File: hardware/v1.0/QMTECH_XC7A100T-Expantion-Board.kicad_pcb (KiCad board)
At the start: 4 copper layers, 98.2 x 98.2 mm, 117 parts, among them J1 Conn_01x34, J2 Conn_01x03, J3 Conn_01x04, J4 Conn_01x03, J5 Conn_01x34, J6 Conn_01x34, J7 Conn_01x34, J9 Conn_01x06, U2 AMS1117-1.8, U3 ADV7180BCP32Z-RL, U4 TLV62585, U5 74LVC245A, U6 TLV62585, U7 74LVC245A, U8 74LVC245A, U9 74LVC245A, Y1 28.63636MHz

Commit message: backup
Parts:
- removed D4: GREEN, LED_SMD:LED_0402_1005Metric_Pad0.77x0.64mm_HandSolder
- removed J1: Conn_01x34, C279718:FPC-SMD_KH-FG0.5-H2.0-34PIN
- removed J3: Conn_01x04, Connector_PinHeader_2.54mm:PinHeader_1x04_P2.54mm_Vertical
- removed RN21, RN22, RN23, RN24, RN27, RN28, RN29, RN30, RN31, RN32, RN33, RN34: 270, Resistor_SMD:R_Array_Convex_4x0603
- removed RN25, RN26: 540, Resistor_SMD:R_Array_Convex_4x0603
- added C36: 22uf, Capacitor_SMD:C_0805_2012Metric, F.Cu at (165.3, 117.7)
- added C37: 22uf, Capacitor_SMD:C_0805_2012Metric, F.Cu at (165.3, 120.7)
- added C38: 10nf, Capacitor_SMD:C_0603_1608Metric, F.Cu at (158.0, 175.1)
- added C39: 22uf, Capacitor_SMD:C_0805_2012Metric, F.Cu at (165.3, 123.7)
- added J10: Conn_01x06, Connector_PinHeader_2.54mm:PinHeader_1x06_P2.54mm_Vertical, F.Cu at (78.7, 136.5)
- added J11: Conn_01x04, Connector_PinHeader_2.54mm:PinHeader_1x04_P2.54mm_Vertical, F.Cu at (129.5, 111.8)
- added J12: Conn_01x34, C279718:FPC-SMD_KH-FG0.5-H2.0-34PIN, F.Cu at (142.9, 113.6)
- added J13: Conn_02x10_Odd_Even, Connector_PinSocket_2.54mm:PinSocket_2x10_P2.54mm_Vertical, F.Cu at (154.8, 136.5)
- added J8: Conn_01x34, C279718:FPC-SMD_KH-FG0.5-H2.0-34PIN, F.Cu at (110.9, 113.7)
- added L3: 1uh, Inductor_SMD:L_0603_1608Metric, F.Cu at (169.5, 117.5)
- added R24: 270, Resistor_SMD:R_0603_1608Metric, F.Cu at (-18.8, 143.9)
- added R25: 270, Resistor_SMD:R_0603_1608Metric, F.Cu at (-22.6, 201.8)
- added R26: 270, Resistor_SMD:R_0603_1608Metric, F.Cu at (-22.6, 204.3)
- added R27: 270, Resistor_SMD:R_0603_1608Metric, F.Cu at (-21.0, 172.7)
- added R28: 4.7K, Resistor_SMD:R_0603_1608Metric, B.Cu at (132.5, 114.3)
- added R29: 4.7K, Resistor_SMD:R_0603_1608Metric, B.Cu at (132.5, 116.8)
- added R30: 270, Resistor_SMD:R_0603_1608Metric, F.Cu at (158.0, 182.7)
- added R31: 450K, Resistor_SMD:R_0402_1005Metric, F.Cu at (169.0, 119.7)
- added R32: 100K, Resistor_SMD:R_0402_1005Metric, F.Cu at (169.0, 121.7)
- added R33: 20, Resistor_SMD:R_0603_1608Metric, F.Cu at (170.6, 176.9)
- added U10: 74LVC245A, Package_SO:TSSOP-20_4.4x6.5mm_P0.65mm, F.Cu at (77.1, 123.2)
- added U11: TLV62585, Package_TO_SOT_SMD:SOT-563, F.Cu at (171.3, 124.8)
- C10, C17: value 10nf -> 22uf; footprint Capacitor_SMD:C_0603_1608Metric -> Capacitor_SMD:C_0805_2012Metric
- C11: value 82nf -> 0.1uf
- C13, C14: value 0.1uf -> 10nf
- C19: value 10nf -> 82nf
- C2, C3: value 0.1uf -> 47pf
- C21: value 22uf -> 0.1uf; footprint Capacitor_SMD:C_0805_2012Metric -> Capacitor_SMD:C_0603_1608Metric
- C22: value 22uf -> 10nf; footprint Capacitor_SMD:C_0805_2012Metric -> Capacitor_SMD:C_0603_1608Metric
- C25, C26, C27, C28, C29, L2: moved to B.Cu
- C5, C6: value 47pf -> 0.1uf; moved to B.Cu
- D2: value LED -> GREEN; footprint LED_SMD:LED_0805_2012Metric -> LED_SMD:LED_0402_1005Metric_Pad0.77x0.64mm_HandSolder
- D3: value GREEN -> LED; footprint LED_SMD:LED_0402_1005Metric_Pad0.77x0.64mm_HandSolder -> LED_SMD:LED_0805_2012Metric
- J2, J4: value Conn_01x03 -> Conn_01x34; footprint Connector_PinHeader_2.54mm:PinHeader_1x03_P2.54mm_Vertical -> C279718:FPC-SMD_KH-FG0.5-H2.0-34PIN
- J5, J6: value Conn_01x34 -> Conn_01x03; footprint C279718:FPC-SMD_KH-FG0.5-H2.0-34PIN -> Connector_PinHeader_2.54mm:PinHeader_1x03_P2.54mm_Vertical
- J7: value Conn_01x34 -> Conn_01x04; footprint C279718:FPC-SMD_KH-FG0.5-H2.0-34PIN -> Connector_PinHeader_2.54mm:PinHeader_1x04_P2.54mm_Vertical
- J9: value Conn_01x06 -> Conn_01x34; footprint Connector_PinHeader_2.54mm:PinHeader_1x06_P2.54mm_Vertical -> C279718:FPC-SMD_KH-FG0.5-H2.0-34PIN
- R1, R2: value 36 -> 4.7K; footprint Resistor_SMD:R_0603_1608Metric -> Resistor_SMD:R_0603_1608Metric_Pad0.98x0.95mm_HandSolder
- R10: value 450K -> 36; footprint Resistor_SMD:R_0402_1005Metric -> Resistor_SMD:R_0603_1608Metric; moved to B.Cu
- R11: value 100K -> 39; footprint Resistor_SMD:R_0402_1005Metric -> Resistor_SMD:R_0603_1608Metric; moved to B.Cu
- R12: value 100 -> 39; moved to B.Cu
- R13: value 100 -> 270
- R14: value 1K -> 1.69k
- R15: value 10K -> 450K; footprint Resistor_SMD:R_0603_1608Metric -> Resistor_SMD:R_0402_1005Metric
- R16: value 450K -> 100K
- R17: value 100K -> 100; footprint Resistor_SMD:R_0402_1005Metric -> Resistor_SMD:R_0603_1608Metric; moved to B.Cu
- R18: value 270 -> 100; moved to B.Cu
- R19: value 270 -> 1K
- R20: value 270 -> 450K; footprint Resistor_SMD:R_0603_1608Metric -> Resistor_SMD:R_0402_1005Metric; moved to B.Cu
- R21: value 270 -> 100K; footprint Resistor_SMD:R_0603_1608Metric -> Resistor_SMD:R_0402_1005Metric; moved to B.Cu
- R3, R4: value 39 -> 4.7K; footprint Resistor_SMD:R_0603_1608Metric -> Resistor_SMD:R_0603_1608Metric_Pad0.98x0.95mm_HandSolder
- R5: value 10K -> 4.7K; footprint Resistor_SMD:R_0603_1608Metric -> Resistor_SMD:R_0603_1608Metric_Pad0.98x0.95mm_HandSolder
- R6, R7: value 270 -> 4.7K; footprint Resistor_SMD:R_0603_1608Metric -> Resistor_SMD:R_0603_1608Metric_Pad0.98x0.95mm_HandSolder
- R8: value 270 -> 10K
- R9: value 1.69k -> 36; moved to B.Cu
- RN10, RN13, RN14, RN9: value 270 -> 540
- RN15, RN16: value 540 -> 270
- RN17, RN18, RN19, RN20: value 270 -> 0
- U2: value AMS1117-1.8 -> CP2102N-Axx-xQFN24; footprint Package_TO_SOT_SMD:SOT-223-3_TabPin2 -> Package_DFN_QFN:QFN-24-1EP_4x4mm_P0.5mm_EP2.6x2.6mm
- U3: value ADV7180BCP32Z-RL -> AMS1117-1.8; footprint Package_CSP:LFCSP-32-1EP_5x5mm_P0.5mm_EP3.6x3.6mm -> Package_TO_SOT_SMD:SOT-223-3_TabPin2
- U4: value TLV62585 -> ADV7180BCP32Z-RL; footprint Package_TO_SOT_SMD:SOT-563 -> Package_CSP:LFCSP-32-1EP_5x5mm_P0.5mm_EP3.6x3.6mm
- U5: value 74LVC245A -> TLV62585; footprint Package_SO:TSSOP-20_4.4x6.5mm_P0.65mm -> Package_TO_SOT_SMD:SOT-563
- U6: value TLV62585 -> 74LVC245A; footprint Package_TO_SOT_SMD:SOT-563 -> Package_SO:TSSOP-20_4.4x6.5mm_P0.65mm; moved to B.Cu
- U7: value 74LVC245A -> TLV62585; footprint Package_SO:TSSOP-20_4.4x6.5mm_P0.65mm -> Package_TO_SOT_SMD:SOT-563; moved to B.Cu
- moved C30 293.2 mm to (-18.8, 136.4)
- moved C31 293.2 mm to (-18.8, 138.9)
- moved D2 241.2 mm to (11.9, 197.9)
- moved C32 236.5 mm to (-22.6, 196.7)
- moved C33 236.5 mm to (-22.6, 199.2)
- moved R19 232.4 mm to (46.0, 179.7)
- moved C34 232.3 mm to (-21.0, 167.7)
- moved C35 232.3 mm to (-21.0, 170.2)
- moved RN8 223.3 mm to (64.0, 135.4), turned to 90 degrees
- moved R23 220.6 mm to (-18.8, 141.4)
- moved C23 219.5 mm to (46.8, 187.5)
- moved C24 219.5 mm to (46.8, 190.5)
- moved U7 216.8 mm to (64.3, 126.1), turned to 180 degrees
- moved RN14 216.6 mm to (74.4, 129.2), turned to 90 degrees
- moved RN7 215.2 mm to (68.0, 135.4), turned to 90 degrees
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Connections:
- C10 pad 1: +1V8 -> +5V
- C10 pad 2: Net-(U3-ELPF) -> GND
- C11 pad 1: +1V8 -> +3V3
- C11 pad 2: Net-(C11-Pad2) -> GND
- C12 pad 1: +3V3 -> +1V8
- C13 pad 1: +1V8 -> +3V3
- C16 pad 1: +3V3 -> +1V8
- C17 pad 1: +1V8 -> +3V3
- C18 pad 2: GND -> Net-(U4-ELPF)
- C19 pad 2: GND -> Net-(C19-Pad2)
- C2 pad 1: +3V3 -> Net-(U4-XTAL1)
- C20 pad 1: +5V -> +3V3
- C21 pad 1: +3V3 -> +1V8
- C22 pad 1: +3V3 -> +1V8
- C3 pad 1: /ADV7180-board/AIN1 -> Net-(U4-XTAL)
- C3 pad 2: Net-(C3-Pad2) -> GND
- C4 pad 1: /ADV7180-board/AIN2 -> +3V3
- C4 pad 2: Net-(C4-Pad2) -> GND
- C5 pad 1: Net-(U3-XTAL1) -> /ADV7180-board/AIN1
- C5 pad 2: GND -> Net-(C5-Pad2)
- C6 pad 1: Net-(U3-XTAL) -> /ADV7180-board/AIN2
- C6 pad 2: GND -> Net-(C6-Pad2)
- C7 pad 1: +1V8 -> Net-(U4-VREFN)
- C7 pad 2: GND -> Net-(U4-VREFP)
- C8 pad 1: Net-(U3-VREFN) -> +1V8
- C8 pad 2: Net-(U3-VREFP) -> GND
- J2 pad 2: Net-(J2-Pin_2) -> +5V
- J2 pad 3: GND -> +5V
- J4 pad 1: +5V -> GND
- J4 pad 2: Net-(J4-Pin_2) -> /PORT1_CLK
- J4 pad 3: GND -> /PORT1_HS
- J5 pad 1: GND -> +5V
- J5 pad 2: /ADV7180-board/YUV_CLK -> Net-(J5-Pin_2)
- J5 pad 3: /ADV7180-board/YUV_HS -> GND
- J6 pad 1: GND -> +5V
- J6 pad 2: /PORT1_CLK -> Net-(J6-Pin_2)
- J6 pad 3: /PORT1_HS -> GND
- J7 pad 1: +5V -> /ADV7180-board/RST
- J7 pad 2: +5V -> /ADV7180-board/SDATA
- J7 pad 3: +5V -> /ADV7180-board/SCLK
- J7 pad 4: +5V -> GND
- J9 pad 1: /vga-board/VGA_VSYNC -> +5V
- J9 pad 2: /vga-board/VGA_HSYNC -> +5V
- J9 pad 3: /vga-board/BLUE -> +5V
- J9 pad 4: /vga-board/GREEN -> +5V
- J9 pad 5: /vga-board/RED -> GND
- J9 pad 6: GND -> /vga-board/VGA_RED7
- L1 pad 1: Net-(U4-SW) -> Net-(U5-SW)
- L2 pad 1: Net-(U6-SW) -> Net-(U7-SW)
- R1 pad 1: Net-(J2-Pin_2) -> +3V3
- R1 pad 2: Net-(C3-Pad2) -> Net-(J1-DAT2)
- R10 pad 1: Net-(U4-FB) -> Net-(J6-Pin_2)
- R10 pad 2: +3V3 -> Net-(C6-Pad2)
- R11 pad 1: GND -> Net-(C5-Pad2)
- R11 pad 2: Net-(U4-FB) -> GND
- R12 pad 1: Net-(U5-B0) -> Net-(C6-Pad2)
- R12 pad 2: /vga-board/VGA_VSYNC -> GND
- R13 pad 1: Net-(U5-B1) -> Net-(D1-A)
- R13 pad 2: /vga-board/VGA_HSYNC -> +3V3
- R14 pad 1: +3V3 -> Net-(U4-ELPF)
- R14 pad 2: Net-(D3-A) -> Net-(C19-Pad2)
- R15 pad 1: +5V -> Net-(U5-FB)
- R15 pad 2: Net-(D4-A) -> +3V3
- R16 pad 1: Net-(U6-FB) -> GND
- R16 pad 2: +3V3 -> Net-(U5-FB)
- R17 pad 1: GND -> Net-(U6-B0)
- R17 pad 2: Net-(U6-FB) -> /vga-board/VGA_VSYNC
- R18 pad 1: GND -> Net-(U6-B1)
- R18 pad 2: Net-(R18-Pad2) -> /vga-board/VGA_HSYNC
- R19 pad 1: Net-(R18-Pad2) -> +3V3
- R19 pad 2: Net-(RN5-R4.1) -> Net-(D2-A)
- R2 pad 1: Net-(J4-Pin_2) -> +3V3
- R2 pad 2: Net-(C4-Pad2) -> Net-(J1-DAT3/CD)
- R20 pad 1: GND -> Net-(U7-FB)
- R20 pad 2: Net-(R20-Pad2) -> +3V3
- R21 pad 1: Net-(R20-Pad2) -> GND
- R21 pad 2: Net-(RN15-R4.1) -> Net-(U7-FB)
- R23 pad 2: Net-(RN25-R4.1) -> Net-(RN5-R4.1)
- R3 pad 1: Net-(C3-Pad2) -> +3V3
- R3 pad 2: GND -> Net-(J1-CMD)
- R4 pad 1: Net-(C4-Pad2) -> +3V3
- R4 pad 2: GND -> Net-(J1-CLK)
- R5 pad 1: /ADV7180-board/ALSB -> +3V3
- R5 pad 2: +3V3 -> Net-(J1-DAT0)
- R6 pad 1: Net-(D1-A) -> +3V3
- R6 pad 2: +3V3 -> Net-(J1-DAT1)
- R7 pad 1: Net-(D2-A) -> +3V3
- R7 pad 2: Net-(R7-Pad2) -> Net-(J1-DET)
- R8 pad 1: Net-(R7-Pad2) -> /ADV7180-board/ALSB
- R8 pad 2: +5V -> +3V3
- R9 pad 1: Net-(U3-ELPF) -> Net-(J5-Pin_2)
- R9 pad 2: Net-(C11-Pad2) -> Net-(C5-Pad2)
- RN1 pad 1: /ADV7180-board/YUV_P3 -> Net-(J8-Pin_5)
- RN1 pad 2: /ADV7180-board/YUV_P2 -> Net-(J8-Pin_4)
- RN1 pad 3: /ADV7180-board/YUV_P1 -> Net-(J8-Pin_3)
- RN1 pad 4: /ADV7180-board/YUV_P0 -> Net-(J8-Pin_2)
- RN1 pad 5: Net-(RN1-R4.2) -> /ADV7180-board/YUV_CLK
- RN1 pad 6: Net-(RN1-R3.2) -> /ADV7180-board/YUV_HS
- RN1 pad 7: Net-(RN1-R2.2) -> /ADV7180-board/YUV_INTRQ
- RN1 pad 8: Net-(RN1-R1.2) -> /ADV7180-board/YUV_VS
- RN10 pad 1: Net-(RN10A-R1.1) -> Net-(RN10-R1.1)
- RN10 pad 2: (no net) -> Net-(RN10-R2.1)
- RN10 pad 3: (no net) -> Net-(RN10-R3.1)
- RN10 pad 4: (no net) -> Net-(RN10-R4.1)
- RN10 pad 5: (no net) -> Net-(RN10-R4.2)
- RN10 pad 6: (no net) -> Net-(RN10-R3.2)
- RN10 pad 7: (no net) -> Net-(RN10-R2.2)
- RN10 pad 8: Net-(RN10A-R1.2) -> Net-(RN10-R1.2)
- RN11 pad 1: Net-(RN11A-R1.1) -> Net-(RN10-R4.1)
- RN11 pad 2: (no net) -> Net-(RN11A-R1.2)
- RN11 pad 3: (no net) -> Net-(RN11B-R2.2)
- RN11 pad 4: (no net) -> Net-(RN11C-R3.2)
- RN11 pad 5: (no net) -> Net-(RN11D-R4.2)
- RN11 pad 6: (no net) -> Net-(RN11C-R3.2)
- RN11 pad 7: (no net) -> Net-(RN11B-R2.2)
- RN11 pad 8: Net-(RN10A-R1.1) -> Net-(RN11A-R1.2)
- RN12 pad 1: Net-(RN12A-R1.1) -> /vga-board/BLUE
- RN12 pad 2: (no net) -> Net-(RN10-R1.1)
- RN12 pad 3: (no net) -> Net-(RN10-R2.1)
- RN12 pad 4: (no net) -> Net-(RN10-R3.1)
- RN12 pad 5: (no net) -> Net-(RN10-R4.1)
- RN12 pad 6: (no net) -> Net-(RN10-R3.1)
- RN12 pad 7: (no net) -> Net-(RN10-R2.1)
- RN12 pad 8: Net-(RN11A-R1.1) -> Net-(RN10-R1.1)
- RN13 pad 1: Net-(RN13A-R1.1) -> Net-(RN13-R1.1)
- RN13 pad 2: (no net) -> Net-(RN13-R2.1)
- RN13 pad 3: (no net) -> Net-(RN13-R3.1)
- RN13 pad 4: (no net) -> Net-(RN13-R4.1)
- RN13 pad 5: (no net) -> Net-(RN13-R4.2)
- RN13 pad 6: (no net) -> Net-(RN13-R3.2)
- RN13 pad 7: (no net) -> Net-(RN13-R2.2)
- RN13 pad 8: Net-(RN12A-R1.1) -> Net-(RN13-R1.2)
- RN14 pad 1: /vga-board/RED -> Net-(RN14-R1.1)
- RN14 pad 2: (no net) -> Net-(RN14-R2.1)
- RN14 pad 3: (no net) -> Net-(RN14-R3.1)
- RN14 pad 4: (no net) -> Net-(RN14-R4.1)
- RN14 pad 5: (no net) -> Net-(RN14-R4.2)
- RN14 pad 6: (no net) -> Net-(RN14-R3.2)
- RN14 pad 7: (no net) -> Net-(RN14-R2.2)
- RN14 pad 8: Net-(RN13A-R1.1) -> Net-(RN14-R1.2)
- RN15 pad 1: Net-(RN15-R1.1) -> Net-(RN14-R4.1)
- RN15 pad 2: Net-(RN15-R2.1) -> Net-(RN13-R1.1)
- RN15 pad 3: Net-(RN15-R3.1) -> Net-(RN13-R2.1)
- RN15 pad 4: Net-(RN15-R4.1) -> Net-(RN13-R3.1)
- RN15 pad 5: Net-(RN15-R4.2) -> Net-(RN13-R4.1)
- RN15 pad 6: Net-(RN15-R3.2) -> Net-(RN13-R3.1)
- RN15 pad 7: Net-(RN15-R2.2) -> Net-(RN13-R2.1)
- RN15 pad 8: Net-(RN15-R1.2) -> Net-(RN13-R1.1)
- RN16 pad 1: Net-(RN16-R1.1) -> /vga-board/GREEN
- RN16 pad 2: Net-(RN16-R2.1) -> Net-(RN14-R1.1)
- RN16 pad 3: Net-(RN16-R3.1) -> Net-(RN14-R2.1)
- RN16 pad 4: Net-(RN16-R4.1) -> Net-(RN14-R3.1)
- RN16 pad 5: Net-(RN16-R4.2) -> Net-(RN14-R4.1)
- RN16 pad 6: Net-(RN16-R3.2) -> Net-(RN14-R3.1)
- RN16 pad 7: Net-(RN16-R2.2) -> Net-(RN14-R2.1)
- RN16 pad 8: Net-(RN16-R1.2) -> Net-(RN14-R1.1)
- RN17 pad 1: Net-(RN15-R3.1) -> Net-(J12-Pin_5)
- RN17 pad 2: (no net) -> unconnected-(RN17-R2.1-Pad2)
- RN17 pad 3: (no net) -> Net-(J12-Pin_3)
- RN17 pad 4: (no net) -> Net-(J12-Pin_2)
- RN17 pad 5: (no net) -> /OV7725-board/OV7725_CLK
- RN17 pad 6: (no net) -> /OV7725-board/OV7725_HS
- RN17 pad 7: (no net) -> unconnected-(RN17-R2.2-Pad7)
- RN17 pad 8: Net-(RN15-R4.1) -> /OV7725-board/OV7725_VS
- RN18 pad 1: Net-(RN15-R2.1) -> Net-(J12-Pin_21)
- RN18 pad 2: (no net) -> Net-(J12-Pin_20)
- RN18 pad 3: (no net) -> unconnected-(RN18-R3.1-Pad3)
- RN18 pad 4: (no net) -> unconnected-(RN18-R4.1-Pad4)
- RN18 pad 5: (no net) -> unconnected-(RN18-R4.2-Pad5)
- RN18 pad 6: (no net) -> unconnected-(RN18-R3.2-Pad6)
- RN18 pad 7: (no net) -> /OV7725-board/OV7725_P0
- RN18 pad 8: Net-(RN15-R3.1) -> /OV7725-board/OV7725_P1
- RN19 pad 1: Net-(RN15-R1.1) -> Net-(J12-Pin_25)
- RN19 pad 2: (no net) -> Net-(J12-Pin_24)
- RN19 pad 3: (no net) -> Net-(J12-Pin_23)
- RN19 pad 4: (no net) -> Net-(J12-Pin_22)
- RN19 pad 5: (no net) -> /OV7725-board/OV7725_P2
- RN19 pad 6: (no net) -> /OV7725-board/OV7725_P3
- RN19 pad 7: (no net) -> /OV7725-board/OV7725_P4
- RN19 pad 8: Net-(RN15-R2.1) -> /OV7725-board/OV7725_P5
- RN2 pad 1: /ADV7180-board/YUV_P7 -> unconnected-(RN2-R1.1-Pad1)
- RN2 pad 2: /ADV7180-board/YUV_P6 -> unconnected-(RN2-R2.1-Pad2)
- RN2 pad 3: /ADV7180-board/YUV_P5 -> unconnected-(RN2-R3.1-Pad3)
- RN2 pad 4: /ADV7180-board/YUV_P4 -> Net-(J8-Pin_6)
- RN2 pad 5: Net-(RN2-R4.2) -> /ADV7180-board/YUV_SFL
- RN2 pad 6: Net-(RN2-R3.2) -> unconnected-(RN2-R3.2-Pad6)
- RN2 pad 7: Net-(RN2-R2.2) -> unconnected-(RN2-R2.2-Pad7)
- RN2 pad 8: Net-(RN2-R1.2) -> unconnected-(RN2-R1.2-Pad8)
- RN20 pad 1: Net-(RN16-R4.1) -> Net-(J12-Pin_29)
- RN20 pad 2: (no net) -> Net-(J12-Pin_28)
- RN20 pad 3: (no net) -> Net-(J12-Pin_27)
- RN20 pad 4: (no net) -> Net-(J12-Pin_26)
- RN20 pad 5: (no net) -> /OV7725-board/OV7725_P6
- RN20 pad 6: (no net) -> /OV7725-board/OV7725_P7
- RN20 pad 7: (no net) -> /OV7725-board/OV7725_P8
- RN20 pad 8: Net-(RN15-R1.1) -> /OV7725-board/OV7725_P9
- RN3 pad 1: /ADV7180-board/YUV_INTRQ -> Net-(J8-Pin_25)
- RN3 pad 2: /ADV7180-board/YUV_SFL -> Net-(J8-Pin_24)
- RN3 pad 3: /ADV7180-board/YUV_VS -> Net-(J8-Pin_23)
- RN3 pad 4: /ADV7180-board/YUV_HS -> Net-(J8-Pin_22)
- RN3 pad 5: Net-(RN3-R4.2) -> /ADV7180-board/YUV_P0
- RN3 pad 6: Net-(RN3-R3.2) -> /ADV7180-board/YUV_P1
- RN3 pad 7: Net-(RN3-R2.2) -> /ADV7180-board/YUV_P2
- RN3 pad 8: Net-(RN3-R1.2) -> /ADV7180-board/YUV_P3
- RN4 pad 1: /ADV7180-board/YUV_CLK -> Net-(J8-Pin_29)
- RN4 pad 2: unconnected-(RN4-R2.1-Pad2) -> Net-(J8-Pin_28)
- RN4 pad 3: unconnected-(RN4-R3.1-Pad3) -> Net-(J8-Pin_27)
- RN4 pad 4: unconnected-(RN4-R4.1-Pad4) -> Net-(J8-Pin_26)
- RN4 pad 5: unconnected-(RN4-R4.2-Pad5) -> /ADV7180-board/YUV_P4
- RN4 pad 6: unconnected-(RN4-R3.2-Pad6) -> /ADV7180-board/YUV_P5
- RN4 pad 7: unconnected-(RN4-R2.2-Pad7) -> /ADV7180-board/YUV_P6
- RN4 pad 8: Net-(RN4-R1.2) -> /ADV7180-board/YUV_P7
- RN5 pad 1: Net-(RN10A-R1.2) -> Net-(RN5-R1.1)
- RN6 pad 1: Net-(RN13A-R1.1) -> Net-(RN6-R1.1)
- RN6 pad 2: Net-(RN12A-R1.1) -> Net-(RN6-R2.1)
- RN6 pad 3: Net-(RN11A-R1.1) -> Net-(RN6-R3.1)
- RN6 pad 4: Net-(RN10A-R1.1) -> Net-(RN6-R4.1)
- RN7 pad 1: Net-(RN5-R3.1) -> Net-(RN6-R4.1)
- RN7 pad 2: (no net) -> Net-(RN5-R1.1)
- RN7 pad 3: (no net) -> Net-(RN5-R2.1)
- RN7 pad 4: (no net) -> Net-(RN5-R3.1)
- RN7 pad 5: (no net) -> Net-(RN5-R4.1)
- RN7 pad 6: (no net) -> Net-(RN5-R3.1)
- RN7 pad 7: (no net) -> Net-(RN5-R2.1)
- RN7 pad 8: Net-(RN5-R4.1) -> Net-(RN5-R1.1)
- RN8 pad 1: Net-(RN5-R2.1) -> /vga-board/RED
- RN8 pad 2: (no net) -> Net-(RN6-R1.1)
- RN8 pad 3: (no net) -> Net-(RN6-R2.1)
- RN8 pad 4: (no net) -> Net-(RN6-R3.1)
- RN8 pad 5: (no net) -> Net-(RN6-R4.1)
- RN8 pad 6: (no net) -> Net-(RN6-R3.1)
- RN8 pad 7: (no net) -> Net-(RN6-R2.1)
- RN8 pad 8: Net-(RN5-R3.1) -> Net-(RN6-R1.1)
- RN9 pad 1: Net-(RN10A-R1.2) -> Net-(RN11A-R1.2)
- RN9 pad 2: (no net) -> Net-(RN11B-R2.2)
- RN9 pad 3: (no net) -> Net-(RN11C-R3.2)
- RN9 pad 4: (no net) -> Net-(RN11D-R4.2)
- RN9 pad 5: (no net) -> Net-(RN9-R4.2)
- RN9 pad 6: (no net) -> Net-(RN9-R3.2)
- RN9 pad 7: (no net) -> Net-(RN9-R2.2)
- RN9 pad 8: Net-(RN5-R2.1) -> Net-(RN9-R1.2)
- U1 pad 1: unconnected-(U1A-GND-Pad1) -> GND
- U1 pad 125: unconnected-(U1B-GND-Pad125) -> GND
- U1 pad 126: unconnected-(U1B-GND-Pad126) -> GND
- U1 pad 2: unconnected-(U1A-GND-Pad2) -> GND
- U1 pad 5: unconnected-(U1A-GND-Pad5) -> GND
- U1 pad 6: unconnected-(U1A-GND-Pad6) -> GND
- U1 pad 61: unconnected-(U1A-GND-Pad61) -> GND
- U1 pad 62: unconnected-(U1A-GND-Pad62) -> GND
- U1 pad 65: unconnected-(U1B-GND-Pad65) -> GND
- U1 pad 66: unconnected-(U1B-GND-Pad66) -> GND
- U1 pad 69: unconnected-(U1B-GND-Pad69) -> GND
- U1 pad 70: unconnected-(U1B-GND-Pad70) -> GND
- U2 pad 1: GND -> unconnected-(U2-~{RI}/CLK-Pad1)
- U2 pad 2: +1V8 -> Net-(U2-GND-Pad2)
- U2 pad 3: +3V3 -> unconnected-(U2-D+-Pad3)
- U3 pad 1: Net-(RN3-R4.2) -> GND
- U3 pad 2: GND -> +1V8
- U4 pad 1: GND -> /ADV7180-board/YUV_HS
- U4 pad 2: Net-(U4-SW) -> GND
- U4 pad 3: +5V -> +3V3
- U4 pad 4: +5V -> /ADV7180-board/YUV_SFL
- U4 pad 5: Net-(U4-FB) -> /ADV7180-board/YUV_P7
- U4 pad 6: unconnected-(U4-PG-Pad6) -> /ADV7180-board/YUV_P6
- U5 pad 1: +3V3 -> GND
- U5 pad 2: /vga-board/VSYNC -> Net-(U5-SW)
- U5 pad 3: /vga-board/HSYNC -> +5V
- U5 pad 4: GND -> +5V
- U5 pad 5: GND -> Net-(U5-FB)
- U5 pad 6: GND -> unconnected-(U5-PG-Pad6)
- U6 pad 1: GND -> +3V3
- U6 pad 2: Net-(U6-SW) -> /vga-board/VSYNC
- U6 pad 3: +5V -> /vga-board/HSYNC
- U6 pad 4: +5V -> GND
- U6 pad 5: Net-(U6-FB) -> GND
- U6 pad 6: unconnected-(U6-PG-Pad6) -> GND
- U7 pad 1: +3V3 -> GND
- U7 pad 2: /vga-board/VGA_RED0 -> Net-(U7-SW)
- U7 pad 3: /vga-board/VGA_RED1 -> +5V
- U7 pad 4: /vga-board/VGA_RED2 -> +5V
- U7 pad 5: /vga-board/VGA_RED3 -> Net-(U7-FB)
- U7 pad 6: /vga-board/VGA_RED4 -> unconnected-(U7-PG-Pad6)
- U8 pad 11: Net-(RN16-R1.2) -> Net-(RN6-R1.2)
- U8 pad 12: Net-(RN16-R2.2) -> Net-(RN6-R2.2)
- U8 pad 13: Net-(RN16-R3.2) -> Net-(RN6-R3.2)
- U8 pad 14: Net-(RN16-R4.2) -> Net-(RN6-R4.2)
- U8 pad 15: Net-(RN15-R1.2) -> Net-(RN5-R1.2)
- U8 pad 16: Net-(RN15-R2.2) -> Net-(RN5-R2.2)
- U8 pad 17: Net-(RN15-R3.2) -> Net-(RN5-R3.2)
- U8 pad 18: Net-(RN15-R4.2) -> Net-(RN5-R4.2)
- U8 pad 2: /vga-board/VGA_BLUE0 -> /vga-board/VGA_RED0
- U8 pad 3: /vga-board/VGA_BLUE1 -> /vga-board/VGA_RED1
- U8 pad 4: /vga-board/VGA_BLUE2 -> /vga-board/VGA_RED2
- U8 pad 5: /vga-board/VGA_BLUE3 -> /vga-board/VGA_RED3
- U8 pad 6: /vga-board/VGA_BLUE4 -> /vga-board/VGA_RED4
- U8 pad 7: /vga-board/VGA_BLUE5 -> /vga-board/VGA_RED5
- U8 pad 8: /vga-board/VGA_BLUE6 -> /vga-board/VGA_RED6
- U8 pad 9: /vga-board/VGA_BLUE7 -> /vga-board/VGA_RED7
- U9 pad 11: Net-(RN26-R1.2) -> Net-(RN10-R1.2)
- U9 pad 12: Net-(RN26-R2.2) -> Net-(RN10-R2.2)
- U9 pad 13: Net-(RN26-R3.2) -> Net-(RN10-R3.2)
- U9 pad 14: Net-(RN26-R4.2) -> Net-(RN10-R4.2)
- U9 pad 15: Net-(RN25-R1.2) -> Net-(RN9-R1.2)
- U9 pad 16: Net-(RN25-R2.2) -> Net-(RN9-R2.2)
- U9 pad 17: Net-(RN25-R3.2) -> Net-(RN9-R3.2)
- U9 pad 18: Net-(RN25-R4.2) -> Net-(RN9-R4.2)
- U9 pad 2: /vga-board/VGA_GREEN0 -> /vga-board/VGA_BLUE0
- U9 pad 3: /vga-board/VGA_GREEN1 -> /vga-board/VGA_BLUE1
- U9 pad 4: /vga-board/VGA_GREEN2 -> /vga-board/VGA_BLUE2
- U9 pad 5: /vga-board/VGA_GREEN3 -> /vga-board/VGA_BLUE3
- U9 pad 6: /vga-board/VGA_GREEN4 -> /vga-board/VGA_BLUE4
- U9 pad 7: /vga-board/VGA_GREEN5 -> /vga-board/VGA_BLUE5
- U9 pad 8: /vga-board/VGA_GREEN6 -> /vga-board/VGA_BLUE6
- U9 pad 9: /vga-board/VGA_GREEN7 -> /vga-board/VGA_BLUE7
- Y1 pad 1: Net-(U3-XTAL1) -> Net-(U4-XTAL1)
- Y1 pad 3: Net-(U3-XTAL) -> Net-(U4-XTAL)
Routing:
- net /OV7725-board/OV7725_CLK: track 0.00 -> 24.2 mm, vias 0 -> 1
- net /OV7725-board/OV7725_VS: track 0.00 -> 24.1 mm, vias 0 -> 1
- net /OV7725-board/OV7725_P1: track 0.00 -> 22.2 mm
- net /OV7725-board/OV7725_HS: track 0.00 -> 21.5 mm, vias 0 -> 1
- net /ADV7180-board/YUV_P7: track 0.00 -> 21.3 mm
- net /ADV7180-board/YUV_P6: track 0.00 -> 20.1 mm
- net /OV7725-board/OV7725_P3: track 0.00 -> 19.6 mm
- net /OV7725-board/OV7725_P0: track 0.00 -> 19.4 mm
- net /OV7725-board/OV7725_P5: track 0.00 -> 19.2 mm
- net /OV7725-board/OV7725_P7: track 0.00 -> 19.1 mm
- net /ADV7180-board/YUV_P5: track 0.00 -> 18.7 mm
- net /OV7725-board/OV7725_P9: track 0.00 -> 18.7 mm
- net /ADV7180-board/YUV_P4: track 0.00 -> 17.4 mm
- net /ADV7180-board/YUV_P3: track 0.00 -> 17.0 mm
- net /ADV7180-board/YUV_P2: track 0.00 -> 17.0 mm
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- added copper zone on F.Cu, net GND
- added copper zone on In1.Cu, net GND
- added copper zone on In2.Cu, net GND
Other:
- board size 98.2 x 98.2 mm -> 99.1 x 98.5 mm
- board text added: "stackup used is JLC04161H-3313 by jlcpcb"

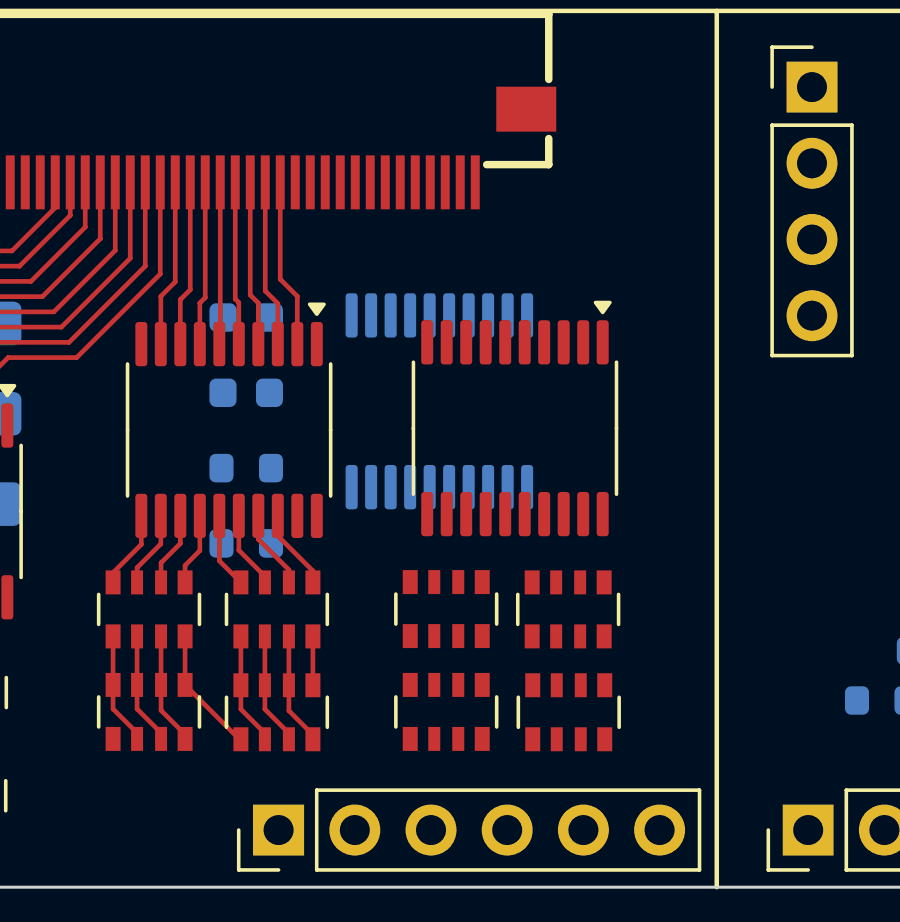
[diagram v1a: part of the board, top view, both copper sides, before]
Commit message: updated project to Kicad version 9.0
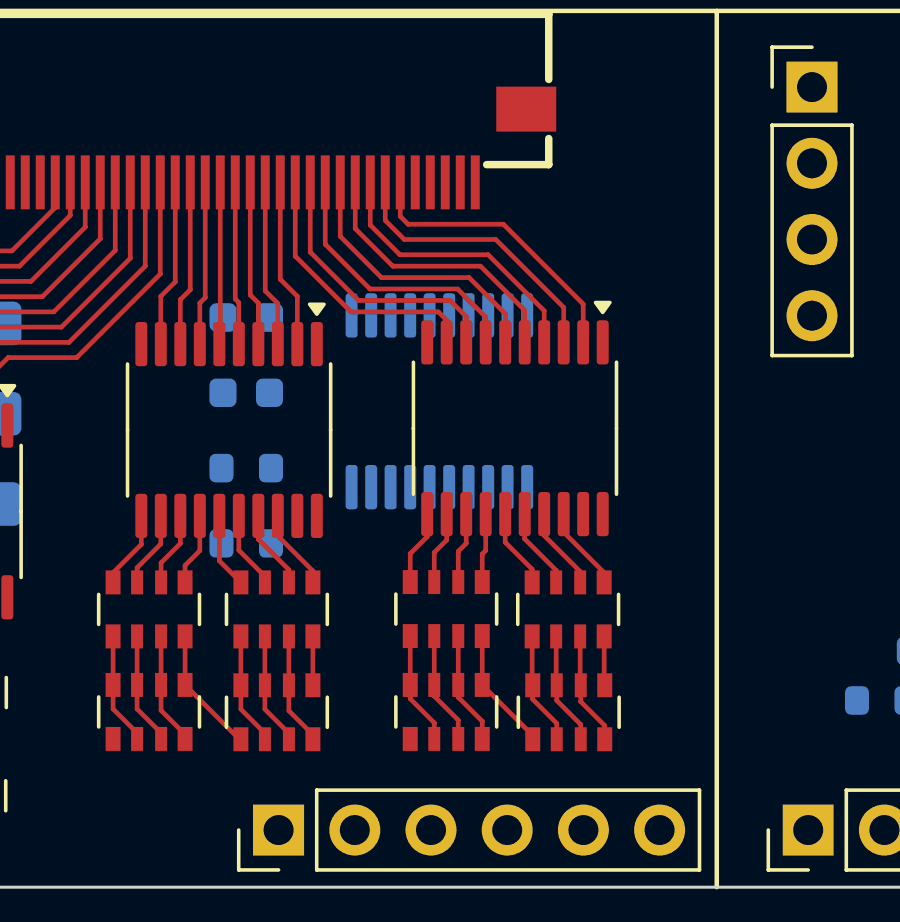
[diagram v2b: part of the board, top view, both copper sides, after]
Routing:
- net /vga-board/VGA_BLUE0: track 0.00 -> 9.72 mm
- net /vga-board/VGA_BLUE1: track 0.00 -> 9.58 mm
- net /vga-board/VGA_BLUE2: track 0.00 -> 9.46 mm
- net /vga-board/VGA_BLUE3: track 0.00 -> 9.39 mm
- net /vga-board/VGA_BLUE4: track 0.00 -> 9.32 mm
- net /vga-board/VGA_BLUE6: track 0.00 -> 9.27 mm
- net /vga-board/VGA_BLUE5: track 0.00 -> 9.26 mm
- net /vga-board/VGA_BLUE7: track 0.00 -> 9.13 mm
- net Net-(RN10-R4.1): track 0.00 -> 4.14 mm
- net Net-(RN11C-R3.2): track 0.00 -> 3.77 mm
- net Net-(RN11A-R1.2): track 0.00 -> 3.77 mm
- net Net-(RN11B-R2.2): track 0.00 -> 3.77 mm
- net Net-(RN10-R3.1): track 0.00 -> 3.76 mm
- net Net-(RN10-R2.1): track 0.00 -> 3.76 mm
- net Net-(RN10-R1.1): track 0.00 -> 3.76 mm
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
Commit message: changes
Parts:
- added C40: 0.1uf, Capacitor_SMD:C_0603_1608Metric, B.Cu at (106.8, 114.9)
- added C41: 0.1uf, Capacitor_SMD:C_0603_1608Metric, B.Cu at (140.3, 114.6)
- added J3: USB_C_Receptacle_USB2.0_16P, Connector_USB:USB_C_Receptacle_Palconn_UTC16-G, F.Cu at (65.4, 92.7)
- added R36: 4.7K, Resistor_SMD:R_0603_1608Metric, B.Cu at (101.6, 117.9)
- added R37: 4.7K, Resistor_SMD:R_0603_1608Metric, B.Cu at (100.4, 119.5)
- added TP1: VCC_PAD, TestPoint:TestPoint_Pad_D1.5mm, B.Cu at (124.8, 113.3)
- added TP2: SWIO_PAD, TestPoint:TestPoint_Pad_D1.5mm, B.Cu at (124.8, 116.8)
- added TP3: GND_PAD, TestPoint:TestPoint_Pad_D1.5mm, B.Cu at (124.8, 120.4)
- added TP4: VCC_PAD, TestPoint:TestPoint_Pad_D1.5mm, B.Cu at (157.7, 113.2)
- added TP5: SWIO_PAD, TestPoint:TestPoint_Pad_D1.5mm, B.Cu at (157.7, 116.7)
- added TP6: GND_PAD, TestPoint:TestPoint_Pad_D1.5mm, B.Cu at (157.7, 120.3)
- added U12: CH32V003JxMx, Package_SO:SOP-8_3.9x4.9mm_P1.27mm, B.Cu at (135.7, 113.9)
- added U2: CH32V003JxMx, Package_SO:SOP-8_3.9x4.9mm_P1.27mm, B.Cu at (102.1, 114.2)
- C1, C10, C17, C20, C4, C8, C9, L1, R15, R16, U3, U5: moved to B.Cu
- moved C32 136.4 mm to (90.8, 121.0), turned to 90 degrees
- moved C33 136.1 mm to (90.8, 124.1), turned to 90 degrees
- moved C35 112.0 mm to (80.5, 122.9), turned to 90 degrees
- moved C34 109.7 mm to (80.5, 126.1), turned to 90 degrees
- moved U5 106.5 mm to (112.1, 114.9)
- moved R16 105.8 mm to (114.6, 113.8), turned to 90 degrees
- moved C10 103.0 mm to (111.7, 112.8)
- moved C20 102.6 mm to (112.6, 119.4)
- moved C17 101.8 mm to (112.6, 117.2)
- moved R15 101.7 mm to (115.4, 116.1), turned to 90 degrees
- moved L1 98.8 mm to (109.9, 115.7), turned to -90 degrees
- moved C4 98.7 mm to (110.0, 120.3), turned to -90 degrees
- moved C1 97.8 mm to (112.5, 121.5)
- moved C9 97.1 mm to (113.4, 125.3), turned to -90 degrees
- moved C8 96.0 mm to (111.5, 125.5), turned to -90 degrees
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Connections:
- U1 pad 10: unconnected-(U1A-B15_E25-Pad10) -> /PORT0_DE
- U1 pad 101: unconnected-(U1B-IO_L5-Pad101) -> /PORT1_BLUE1
- U1 pad 103: unconnected-(U1B-IO_M4-Pad103) -> /PORT1_BLUE3
- U1 pad 105: unconnected-(U1B-IO_N3-Pad105) -> /PORT1_BLUE5
- U1 pad 107: unconnected-(U1B-IO_M6-Pad107) -> /PORT1_BLUE7
- U1 pad 109: unconnected-(U1B-IO_K1-Pad109) -> /PORT1_GREEN1
- U1 pad 11: unconnected-(U1A-B15_G26-Pad11) -> /PORT0_BLUE1
- U1 pad 111: unconnected-(U1B-IO_R3-Pad111) -> /PORT1_GREEN3
- U1 pad 113: unconnected-(U1B-IO_T4-Pad113) -> /PORT1_GREEN5
- U1 pad 115: unconnected-(U1B-IO_P6-Pad115) -> /PORT1_GREEN7
- U1 pad 117: unconnected-(U1B-IO_N3-Pad117) -> /PORT1_RED1
- U1 pad 119: unconnected-(U1B-IO_N1-Pad119) -> /PORT1_RED3
- U1 pad 12: unconnected-(U1A-B15_H26-Pad12) -> /PORT0_BLUE0
- U1 pad 121: unconnected-(U1B-IO_T2-Pad121) -> /PORT1_RED5
- U1 pad 123: unconnected-(U1B-IO_U2-Pad123) -> /PORT1_RED7
- U1 pad 127: unconnected-(U1B-VIN-Pad127) -> /V_USB
- U1 pad 128: unconnected-(U1B-VIN-Pad128) -> /V_USB
- U1 pad 13: unconnected-(U1A-B15_E23-Pad13) -> /PORT0_BLUE3
- U1 pad 14: unconnected-(U1A-B15_F23-Pad14) -> /PORT0_BLUE2
- U1 pad 15: unconnected-(U1A-B15_F22-Pad15) -> /PORT0_BLUE5
- U1 pad 16: unconnected-(U1A-B15_G22-Pad16) -> /PORT0_BLUE4
- U1 pad 17: unconnected-(U1A-B15_J26-Pad17) -> /PORT0_BLUE7
- U1 pad 18: unconnected-(U1A-B15_J25-Pad18) -> /PORT0_BLUE6
- U1 pad 19: unconnected-(U1A-B15_G21-Pad19) -> /PORT0_GREEN1
- U1 pad 20: unconnected-(U1A-B15_G20-Pad20) -> /PORT0_GREEN0
- U1 pad 21: unconnected-(U1A-B15_H22-Pad21) -> /PORT0_GREEN3
- U1 pad 22: unconnected-(U1A-B15_H21-Pad22) -> /PORT0_GREEN2
- U1 pad 23: unconnected-(U1A-B15_J21-Pad23) -> /PORT0_GREEN5
- U1 pad 24: unconnected-(U1A-B15_K21-Pad24) -> /PORT0_GREEN4
- U1 pad 25: unconnected-(U1A-B14_K26-Pad25) -> /PORT0_GREEN7
- U1 pad 26: unconnected-(U1A-B14_K25-Pad26) -> /PORT0_GREEN6
- U1 pad 27: unconnected-(U1A-B15_K23-Pad27) -> /PORT0_RED1
- U1 pad 28: unconnected-(U1A-B15_K22-Pad28) -> /PORT0_RED0
- U1 pad 29: unconnected-(U1A-B14_M26-Pad29) -> /PORT0_RED3
- U1 pad 30: unconnected-(U1A-B14_N26-Pad30) -> /PORT0_RED2
- U1 pad 31: unconnected-(U1A-B14_L23-Pad31) -> /PORT0_RED5
- U1 pad 32: unconnected-(U1A-B14_L22-Pad32) -> /PORT0_RED4
- U1 pad 33: unconnected-(U1A-B14_P26-Pad33) -> /PORT0_RED7
- U1 pad 34: unconnected-(U1A-B14_R26-Pad34) -> /PORT0_RED6
- U1 pad 63: unconnected-(U1A-VIN-Pad63) -> /V_USB
- U1 pad 64: unconnected-(U1A-VIN-Pad64) -> /V_USB
- U1 pad 7: unconnected-(U1A-B15_D26-Pad7) -> /PORT0_HS
- U1 pad 8: unconnected-(U1A-B15_E26-Pad8) -> /PORT0_CLK
- U1 pad 9: unconnected-(U1A-B15_D25-Pad9) -> /PORT0_VS
- U1 pad 97: unconnected-(U1B-IO_H9-Pad97) -> /PORT1_HS
- U1 pad 99: unconnected-(U1B-IO_M2-Pad99) -> /PORT1_VS
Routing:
- net /PORT0_RED6: track 0.00 -> 63.3 mm
- net /PORT0_RED7: track 0.00 -> 62.1 mm
- net /PORT0_RED4: track 0.00 -> 59.6 mm
- net /PORT0_RED5: track 0.00 -> 58.3 mm
- net /PORT0_RED2: track 0.00 -> 56.2 mm
- net /PORT0_RED3: track 0.00 -> 54.7 mm
- net /PORT0_RED0: track 0.00 -> 52.2 mm
- net /PORT0_RED1: track 0.00 -> 51.0 mm
- net /PORT0_GREEN6: track 0.00 -> 48.9 mm
- net /PORT0_GREEN7: track 0.00 -> 47.5 mm
- net /PORT0_GREEN4: track 0.00 -> 46.0 mm
- net /PORT0_GREEN5: track 0.00 -> 44.3 mm
- net /PORT0_GREEN2: track 0.00 -> 42.7 mm
- net /PORT0_GREEN3: track 0.00 -> 41.3 mm
- net /OV7725-board/SDATA: track 0.00 -> 39.7 mm
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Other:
- board text added: "gnd"
- board text added: "swio"
- board text added: "vcc"

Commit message: changes
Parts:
- removed C21: 0.1uf, Capacitor_SMD:C_0603_1608Metric
- removed C22: 10nf, Capacitor_SMD:C_0603_1608Metric
- removed the U2 at (236.7, 106.0)
- added J1: Micro_SD_Card_Det1, C393941:TF-SMD_TF-PUSH, F.Cu at (150.5, 58.7)
- C11, C12, C13, C14, C15, C16: moved to B.Cu
- R15, R16, R20, R21, R31, R32: footprint Resistor_SMD:R_0402_1005Metric -> Resistor_SMD:R_0603_1608Metric
- moved R7 99.2 mm to (141.2, 65.0)
- moved R6 98.7 mm to (141.2, 63.5)
- moved R5 98.1 mm to (141.2, 62.0)
- moved R4 97.6 mm to (141.2, 60.5)
- moved R3 97.1 mm to (141.2, 58.9)
- moved R2 96.6 mm to (141.2, 57.4)
- moved R1 96.1 mm to (141.2, 55.9)
- moved C18 71.9 mm to (107.4, 123.5), turned to -90 degrees
- moved C16 64.4 mm to (106.1, 128.5), turned to -45 degrees
- moved C14 63.0 mm to (106.0, 124.9), turned to 135 degrees
- moved R14 62.0 mm to (105.2, 124.3), turned to 180 degrees
- moved C15 60.6 mm to (104.7, 129.5), turned to -45 degrees
- moved C19 56.6 mm to (105.2, 122.8)
- moved C12 56.1 mm to (108.3, 127.7), turned to -45 degrees
- moved C13 53.1 mm to (110.3, 134.2), turned to -135 degrees
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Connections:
- J10 pad 1: /vga-board/VGA_VSYNC -> /vga-board/VSYNC
- J10 pad 2: /vga-board/VGA_HSYNC -> /vga-board/HSYNC
- J9 pad 30: /vga-board/VSYNC -> /vga-board/VGA_VSYNC
- J9 pad 32: /vga-board/HSYNC -> /vga-board/VGA_HSYNC
- R1 pad 2: Net-(J1-DAT2) -> /SD_DAT2
- R17 pad 2: /vga-board/VGA_VSYNC -> /vga-board/VSYNC
- R18 pad 2: /vga-board/VGA_HSYNC -> /vga-board/HSYNC
- R2 pad 2: Net-(J1-DAT3/CD) -> /SD_DAT3
- R3 pad 2: Net-(J1-CMD) -> /SD_CMD
- R4 pad 2: Net-(J1-CLK) -> /SD_CLK
- R5 pad 2: Net-(J1-DAT0) -> /SD_DAT0
- R6 pad 2: Net-(J1-DAT1) -> /SD_DAT1
- R7 pad 2: Net-(J1-DET) -> /SD_DET
- U1 pad 54: unconnected-(U1A-B13_AB24-Pad54) -> /SD_DAT2
- U1 pad 55: unconnected-(U1A-B13_Y21-Pad55) -> /SD_DAT3
- U1 pad 56: unconnected-(U1A-B13_W21-Pad56) -> /SD_CMD
- U1 pad 57: unconnected-(U1A-B13_Y26-Pad57) -> /SD_CLK
- U1 pad 58: unconnected-(U1A-B13_W25-Pad58) -> /SD_DAT0
- U1 pad 59: unconnected-(U1A-B13_AC26-Pad59) -> /SD_DAT1
- U1 pad 60: unconnected-(U1A-B13_AB26-Pad60) -> /SD_DET
- U6 pad 2: /vga-board/VSYNC -> /vga-board/VGA_VSYNC
- U6 pad 3: /vga-board/HSYNC -> /vga-board/VGA_HSYNC
- U6 pad 4: GND -> unconnected-(U6-A2-Pad4)
- U6 pad 5: GND -> unconnected-(U6-A3-Pad5)
- U6 pad 6: GND -> unconnected-(U6-A4-Pad6)
- U6 pad 7: GND -> unconnected-(U6-A5-Pad7)
- U6 pad 8: GND -> unconnected-(U6-A6-Pad8)
- U6 pad 9: GND -> unconnected-(U6-A7-Pad9)
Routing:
- net +3V3: track 0.00 -> 115.2 mm, vias 0 -> 37
- net /PORT0_RED6: track 63.3 -> 3.63 mm
- net +5V: track 0.00 -> 58.4 mm, vias 0 -> 17
- net /PORT0_RED5: track 58.3 -> 0.46 mm
- net GND: track 16.9 -> 73.3 mm, vias 4 -> 48
- net /PORT0_RED4: track 59.6 -> 3.81 mm
- net /PORT0_RED3: track 54.7 -> 0.81 mm
- net /PORT0_RED2: track 56.2 -> 3.97 mm
- net /PORT0_RED1: track 51.0 -> 0.76 mm
- net /PORT0_RED0: track 52.2 -> 3.76 mm
- net /PORT0_GREEN7: track 47.5 -> 0.61 mm
- net /PORT0_GREEN6: track 48.9 -> 3.64 mm
- net /PORT0_GREEN4: track 46.0 -> 1.93 mm
- net /PORT0_GREEN5: track 44.3 -> 0.61 mm
- net /PORT0_GREEN3: track 41.3 -> 0.36 mm
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- added copper zone on B.Cu, net +1V8
- added copper zone on B.Cu, net +3V3
- added copper zone on F.Cu, net +3V3
- added copper zone on In2.Cu, net +3V3
- added copper zone on B.Cu, net +5V
- added copper zone on F.Cu, net +5V
- added copper zone on In2.Cu, net +5V
- added copper zone on B.Cu, net GND
- added copper zone on B.Cu, net Net-(U5-SW)
- added copper zone on B.Cu, net Net-(U7-SW)

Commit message: backup
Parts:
- removed C17, C29, C37: 22uf, Capacitor_SMD:C_0805_2012Metric
- removed C23, C24: 10uf, Capacitor_SMD:C_0805_2012Metric
- C10, C27, C36: value 22uf -> 4.7uf
- C20, C28, C39: value 22uf -> 10uf
- D1: value LED -> ~; footprint LED_SMD:LED_0805_2012Metric -> C779813:LED-SMD_4P-L1.6-W1.5-BR_TZ-P4-1615
- L1, L2, L3: value 1uh -> 2.2uh
- moved R25 134.1 mm to (91.1, 130.9), turned to -90 degrees
- moved R26 128.5 mm to (81.0, 128.3), turned to -90 degrees
- moved R24 111.2 mm to (91.1, 127.8), turned to -90 degrees
- moved R27 110.1 mm to (81.0, 131.4), turned to -90 degrees
- moved R23 89.3 mm to (70.1, 133.7), turned to -90 degrees
- moved R22 86.2 mm to (70.1, 130.6), turned to -90 degrees
- moved D1 71.3 mm to (125.0, 111.8)
- moved J4 6.89 mm to (155.4, 81.4)
- moved C20 1.98 mm to (99.2, 125.0)
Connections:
- D1 pad 1: GND -> Net-(D1-A)
- D1 pad 2: Net-(D1-A) -> GND
- U2 pad 3: unconnected-(U2-PA2-Pad3) -> /ADV7180-board/STATUS
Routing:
- net +5V: track 58.4 -> 89.4 mm
- net /ADV7180-board/RST: track 6.56 -> 35.7 mm, vias 1 -> 2
- net /ADV7180-board/SCLK: track 11.0 -> 39.2 mm, vias 1 -> 2
- net /ADV7180-board/SDATA: track 11.7 -> 38.0 mm, vias 1 -> 2
- net GND: track 73.3 -> 96.8 mm, vias 48 -> 76
- net /PORT1_RED5: track 19.5 -> 0.00 mm
- net /PORT1_RED7: track 16.7 -> 0.00 mm
- net /PORT1_RED4: track 16.6 -> 0.00 mm
- net /PORT1_RED6: track 13.9 -> 0.00 mm
- net /ADV7180-board/YUV_CLK: track 17.5 -> 28.3 mm
- net /ADV7180-board/YUV_SFL: track 36.8 -> 32.3 mm
- net /ADV7180-board/AIN1: track 7.16 -> 2.81 mm
- net (no net): track 0.00 -> 4.11 mm
- net Net-(J6-Pin_2): track 3.71 -> 0.00 mm
- net Net-(J5-Pin_2): track 3.67 -> 0.00 mm
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
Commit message: changes
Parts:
- moved D2 84.4 mm to (84.9, 155.4)
- moved D3 46.5 mm to (67.7, 152.8)
- moved C38 43.8 mm to (119.3, 154.6)
- moved R30 43.8 mm to (119.3, 162.2)
- moved R33 43.8 mm to (131.9, 156.4)
- moved R19 38.2 mm to (78.7, 160.0)
- moved R13 26.6 mm to (100.1, 155.9)
- moved J4 4.16 mm to (155.4, 77.2)
- moved J1 2.92 mm to (150.2, 55.8)
- moved R1 2.92 mm to (140.9, 53.0)
- moved R2 2.92 mm to (140.9, 54.5)
- moved R5 2.92 mm to (140.9, 59.1)
- moved R6 2.92 mm to (140.9, 60.6)
- moved R7 2.92 mm to (140.9, 62.1)
- moved R3 2.92 mm to (140.9, 56.0)
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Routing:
- net /PORT0_RED6: track 3.63 -> 55.1 mm
- net /PORT0_RED5: track 0.46 -> 50.4 mm
- net /PORT0_RED4: track 3.81 -> 52.0 mm
- net /PORT0_RED3: track 0.81 -> 47.4 mm
- net /PORT0_GREEN6: track 3.64 -> 49.1 mm
- net /PORT0_RED2: track 3.97 -> 49.0 mm
- net /PORT0_GREEN7: track 0.61 -> 45.2 mm
- net /PORT0_RED1: track 0.76 -> 45.0 mm
- net /PORT0_RED0: track 3.76 -> 46.0 mm
- net /PORT0_GREEN2: track 34.9 -> 1.88 mm
- net /PORT0_GREEN1: track 32.0 -> 0.00 mm
- net /PORT0_GREEN0: track 39.3 -> 9.31 mm
- net /SD_DET: track 31.9 -> 3.18 mm
- net /SD_DAT0: track 29.3 -> 3.53 mm
- net /SD_DAT1: track 27.4 -> 3.35 mm
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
